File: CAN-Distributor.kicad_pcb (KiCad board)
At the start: 2 copper layers, 140 x 60 mm, 32 parts, among them J1 3p Terminal Block, J10 RJ10, J11 RJ10, J12 RJ10, J13 4p Terminal Block, J14 4p Terminal Block, J15 4p Terminal Block, J16 RJ10, J2 RJ45_Shielded, J3 RJ45_Shielded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

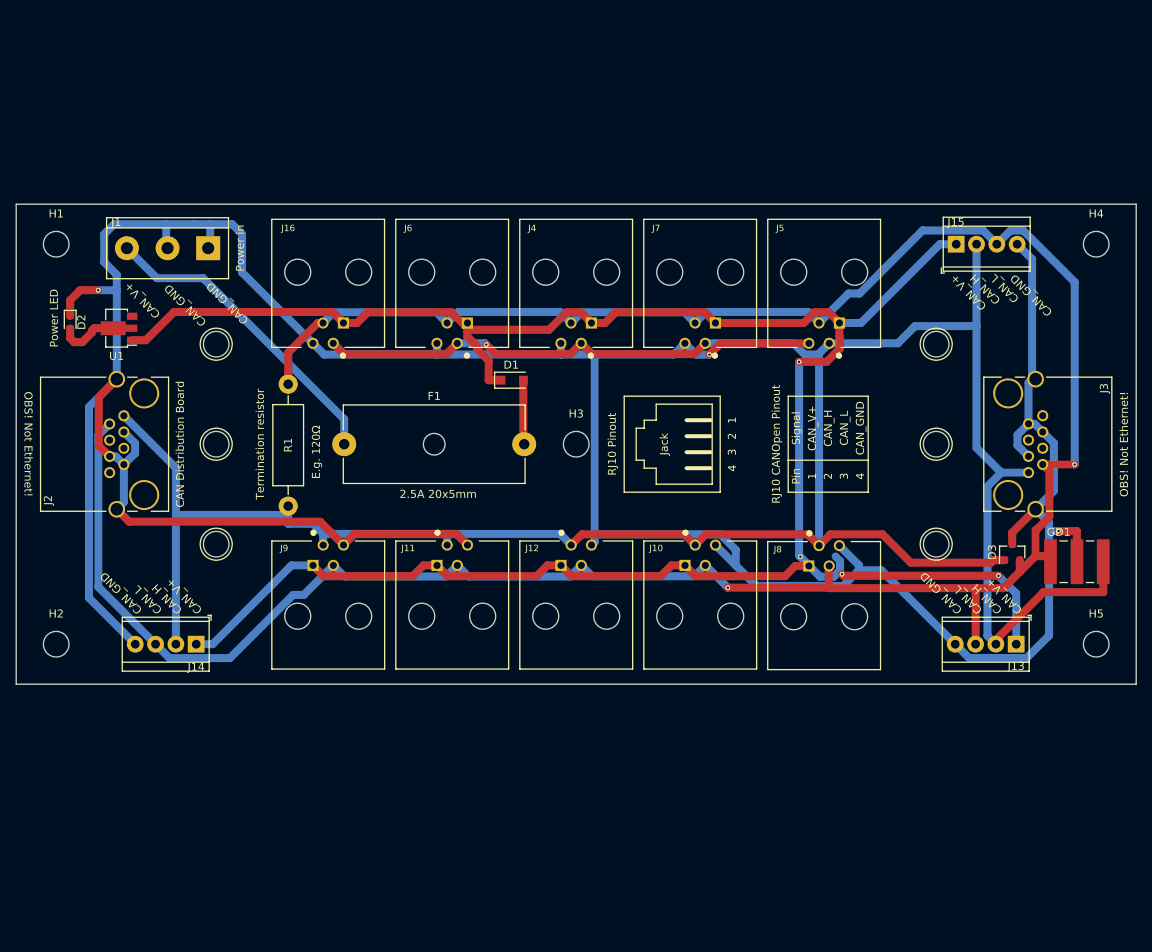
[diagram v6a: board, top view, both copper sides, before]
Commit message: Rotate RJ45 connectors and re-route.
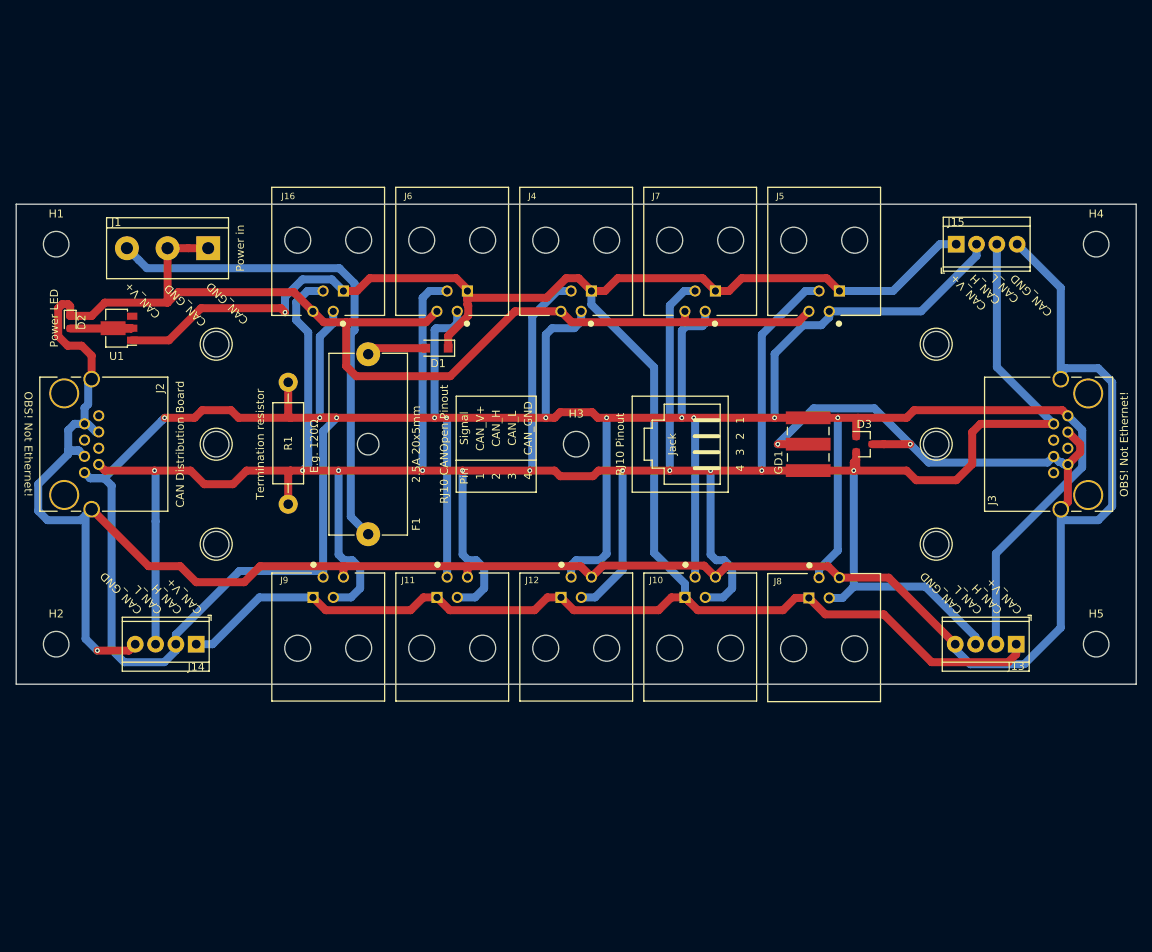
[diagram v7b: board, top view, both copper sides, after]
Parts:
- moved G1 41.5 mm to (117.3, 95.2)
- moved GD1 36.7 mm to (150.3, 95.2), turned to 90 degrees
- moved D3 22.9 mm to (157.3, 95.2), turned to 0 degrees
- moved R1 15.0 mm to (85.3, 102.7), turned to 90 degrees
- moved F1 11.6 mm to (95.3, 106.5), turned to 90 degrees
- moved D1 10.2 mm to (104.0, 83.2), turned to 180 degrees
- moved J3 10.0 mm to (185.3, 95.2), turned to 90 degrees
- moved J2 10.00 mm to (57.4, 95.2), turned to 270 degrees
- moved J8 4.00 mm to (152.3, 120.8)
- moved J10 4.00 mm to (136.8, 120.7)
- moved J11 4.00 mm to (105.8, 120.7)
- moved J12 4.00 mm to (121.3, 120.7)
- moved J16 4.00 mm to (90.3, 69.7)
- moved J4 4.00 mm to (121.3, 69.7)
- moved J5 4.00 mm to (152.3, 69.7)
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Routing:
- net CAN_H: track 331.2 -> 436.8 mm, vias 1 -> 11
- net CAN_L: track 322.8 -> 426.5 mm, vias 2 -> 11
- net CAN_GND: track 415.6 -> 465.4 mm
- net Net-(F1-Pad1): track 39.1 -> 62.7 mm
- net CAN_V+: track 280.7 -> 284.7 mm, vias 4 -> 1
- net Net-(D2-Pad2): track 9.06 -> 10.0 mm
- net Net-(D1-Pad2): track 8.04 -> 7.51 mm
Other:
- board text added: "Erik Almbratt 2021-05-20 2.2 ETA's Github page"
- board text removed: "Erik Almbratt 2021-04-04 2.1 ETA's Github page"
